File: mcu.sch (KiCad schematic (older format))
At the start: 74 parts, among them J10 JTAG, J11 esp32L, J12 esp32B, J13 esp32R, J2 SPI1, J3 uSD, J4 I2C1, J5 serial1, J6 serial2, J7 touch interface, J8 LCD 4.3, J9 EXT_IOS, Q1 ZXMN2F30FH, Q2 ZXMN2F30FH, Q3 ZXMN2F30FH, SW1 reset, SW7 on, U3 AT25SF641, U5 STM32F750Z8, U6 MP3302DJ-LF-P, U7 ESP32-WROOM-32, Y1 25MHz, Y2 32.768 kHz

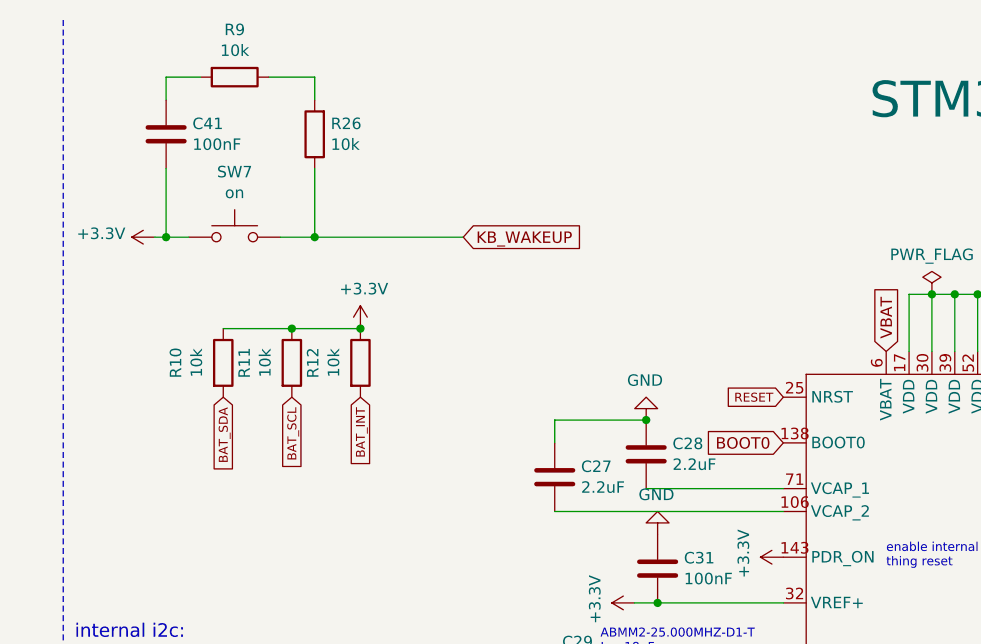
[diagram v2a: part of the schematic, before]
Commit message: Switch matrix to definitive switch
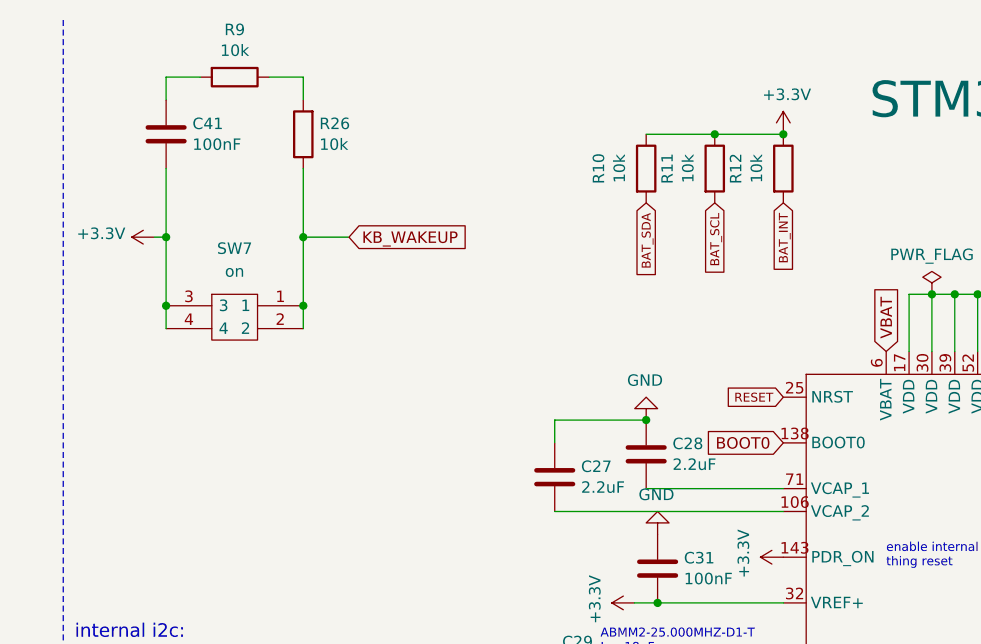
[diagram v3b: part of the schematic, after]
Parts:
- removed SW7: on, Button_Switch_THT:SW_PUSH_6mm, symbol Switch:SW_Push
- added SW7: on, SamacSys_Parts:FSM4JSMATR, symbol SamacSys_Parts:FSM4JSMAATR
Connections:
- net +3V3: now also SW7.3, SW7.4
- net KB_WAKEUP: now also SW7.1, SW7.2
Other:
- moved on the sheet: R10, R11, R12, R26
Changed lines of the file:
@@
 Text Notes 13100 5300 0    39   ~ 0
 USART6_TX
-Text GLabel 10900 2150 3    39   Input ~ 0
+Text GLabel 12750 1300 3    39   Input ~ 0
 BAT_INT
 $Comp
 L Device:R R12
 U 1 1 6021C497
-P 10900 2000
-F 0 "R12" V 10693 2000 50  0000 C CNN
-F 1 "10k" V 10784 2000 50  0000 C CNN
-F 2 "Resistor_SMD:R_0805_2012Metric_Pad1.20x1.40mm_HandSolder" V 10830 2000 50  0001 C CNN
-F 3 "~" H 10900 2000 50  0001 C CNN
-	1    10900 2000
+P 12750 1150
+F 0 "R12" V 12543 1150 50  0000 C CNN
+F 1 "10k" V 12634 1150 50  0000 C CNN
+F 2 "Resistor_SMD:R_0805_2012Metric_Pad1.20x1.40mm_HandSolder" V 12680 1150 50  0001 C CNN
+F 3 "~" H 12750 1150 50  0001 C CNN
+	1    12750 1150
 	1    0    0    -1
 $EndComp
@@
 L power:+3.3V #PWR0139
 U 1 1 6021C91D
-P 10900 1850
-F 0 "#PWR0139" H 10900 1700 50  0001 C CNN
-F 1 "+3.3V" H 10915 2023 50  0000 C CNN
-F 2 "" H 10900 1850 50  0001 C CNN
-F 3 "" H 10900 1850 50  0001 C CNN
-	1    10900 1850
-	1    0    0    -1
-$EndComp
-Text GLabel 10300 2150 3    39   Input ~ 0
+P 12750 1000
+F 0 "#PWR0139" H 12750 850 50  0001 C CNN
+F 1 "+3.3V" H 12765 1173 50  0000 C CNN
+F 2 "" H 12750 1000 50  0001 C CNN
+F 3 "" H 12750 1000 50  0001 C CNN
+	1    12750 1000
+	1    0    0    -1
+$EndComp
+Text GLabel 12150 1300 3    39   Input ~ 0
 BAT_SDA
-Text GLabel 10600 2150 3    39   Input ~ 0
+Text GLabel 12450 1300 3    39   Input ~ 0
 BAT_SCL
 $Comp
 L Device:R R11
 U 1 1 602407FE
-P 10600 2000
-F 0 "R11" V 10393 2000 50  0000 C CNN
-F 1 "10k" V 10484 2000 50  0000 C CNN
-F 2 "Resistor_SMD:R_0805_2012Metric_Pad1.20x1.40mm_HandSolder" V 10530 2000 50  0001 C CNN
-F 3 "~" H 10600 2000 50  0001 C CNN
-	1    10600 2000
+P 12450 1150
+F 0 "R11" V 12243 1150 50  0000 C CNN
+F 1 "10k" V 12334 1150 50  0000 C CNN
+F 2 "Resistor_SMD:R_0805_2012Metric_Pad1.20x1.40mm_HandSolder" V 12380 1150 50  0001 C CNN
+F 3 "~" H 12450 1150 50  0001 C CNN
+	1    12450 1150
 	1    0    0    -1
 $EndComp
@@
 L Device:R R10
 U 1 1 6024B53D
-P 10300 2000
-F 0 "R10" V 10093 2000 50  0000 C CNN
-F 1 "10k" V 10184 2000 50  0000 C CNN
-F 2 "Resistor_SMD:R_0805_2012Metric_Pad1.20x1.40mm_HandSolder" V 10230 2000 50  0001 C CNN
-F 3 "~" H 10300 2000 50  0001 C CNN
-	1    10300 2000
-	1    0    0    -1
-$EndComp
-Wire Wire Line
-	10300 1850 10600 1850
-Connection ~ 10900 1850
-Connection ~ 10600 1850
-Wire Wire Line
-	10600 1850 10900 1850
+P 12150 1150
+F 0 "R10" V 11943 1150 50  0000 C CNN
+F 1 "10k" V 12034 1150 50  0000 C CNN
+F 2 "Resistor_SMD:R_0805_2012Metric_Pad1.20x1.40mm_HandSolder" V 12080 1150 50  0001 C CNN
+F 3 "~" H 12150 1150 50  0001 C CNN
+	1    12150 1150
+	1    0    0    -1
+$EndComp
+Wire Wire Line
+	12150 1000 12450 1000
+Connection ~ 12750 1000
+Connection ~ 12450 1000
+Wire Wire Line
+	12450 1000 12750 1000
 $Comp
 L power:+3.3V #PWR0142
@@
 Text Notes 10550 10900 0    39   ~ 0
 R VF=1.8-2.4 FC=30\nG VF=2.8-3.9 FC=20\nB VF=2.8-3.9 FC=20\nSupply=3.3
-Text GLabel 11350 1450 2    50   Input ~ 0
+Text GLabel 10850 1450 2    50   Input ~ 0
 KB_WAKEUP
-$Comp
-L Switch:SW_Push SW7
-U 1 1 5F9751F4
-P 10350 1450
-F 0 "SW7" H 10350 1735 50  0000 C CNN
-F 1 "on" H 10350 1644 50  0000 C CNN
-F 2 "Button_Switch_THT:SW_PUSH_6mm" H 10350 1650 50  0001 C CNN
-F 3 "~" H 10350 1650 50  0001 C CNN
-	1    10350 1450
-	1    0    0    -1
-$EndComp
 Text Notes 9650 3500 0    59   ~ 0
 internal i2c:\n6BH - Battery charger\nBA/BB or 28/29 - Touch display\n20 - Keyboard matrix output
@@
 L Device:R R26
 U 1 1 5FA5B33C
-P 10700 1000
-F 0 "R26" H 10630 954 50  0000 R CNN
-F 1 "10k" H 10630 1045 50  0000 R CNN
-F 2 "Resistor_SMD:R_0805_2012Metric_Pad1.20x1.40mm_HandSolder" V 10630 1000 50  0001 C CNN
-F 3 "~" H 10700 1000 50  0001 C CNN
-	1    10700 1000
+P 10650 1000
+F 0 "R26" H 10580 954 50  0000 R CNN
+F 1 "10k" H 10580 1045 50  0000 R CNN
+F 2 "Resistor_SMD:R_0805_2012Metric_Pad1.20x1.40mm_HandSolder" V 10580 1000 50  0001 C CNN
+F 3 "~" H 10650 1000 50  0001 C CNN
+	1    10650 1000
 	-1   0    0    1
 $EndComp
@@
 	10000 1450 10050 1450
 Wire Wire Line
-	10550 1450 10700 1450
-Wire Wire Line
-	10500 750  10700 750
-Wire Wire Line
-	10700 750  10700 850
-Wire Wire Line
-	10700 1150 10700 1450
-Connection ~ 10700 1450
-Wire Wire Line
-	10700 1450 11350 1450
-Wire Wire Line
 	10050 1450 10050 1150
-Connection ~ 10050 1450
-Wire Wire Line
-	10050 1450 10150 1450
 Wire Wire Line
 	10050 850  10050 750
@@
 NoConn ~ 15050 3950
 NoConn ~ 12750 6750
+$Comp
+L SamacSys_Parts:FSM4JSMAATR SW7
+U 1 1 5F9A03CF
+P 10050 1750
+F 0 "SW7" H 10350 2000 50  0000 C CNN
+F 1 "on" H 10350 1900 50  0000 C CNN
+F 2 "SamacSys_Parts:FSM4JSMATR" H 11100 1850 50  0001 L CNN
+F 3 "http://www.te.com/commerce/DocumentDelivery/DDEController?Action=showdoc&DocId=Customer+Drawing%7F2-1437565-7%7FV%7Fpdf%7FEnglish%7FENG_CD_2-1437565-7_V.pdf%7F1571563-4" H 11100 1750 50  0001 L CNN
+F 4 "TE CONNECTIVITY / ALCOSWITCH - FSM4JSMAATR - TACTILE SWITCH, SPST-NO, 0.05A, 24V, SMD" H 11100 1650 50  0001 L CNN "Description"
+F 5 "" H 11100 1550 50  0001 L CNN "Height"
+F 6 "TE Connectivity" H 11100 1450 50  0001 L CNN "Manufacturer_Name"
+F 7 "FSM4JSMAATR" H 11100 1350 50  0001 L CNN "Manufacturer_Part_Number"
+F 8 "FSM4JSMAATR" H 11100 1250 50  0001 L CNN "Arrow Part Number"
+F 9 "https://www.arrow.com/en/products/fsm4jsmaatr/te-connectivity" H 11100 1150 50  0001 L CNN "Arrow Price/Stock"
+F 10 "506-FSM4JSMAATR" H 11100 1050 50  0001 L CNN "Mouser Part Number"
+F 11 "https://www.mouser.co.uk/ProductDetail/TE-Connectivity-PB/FSM4JSMAATR?qs=BaILwcusPn8tfgWWpzI4xg%3D%3D" H 11100 950 50  0001 L CNN "Mouser Price/Stock"
+	1    10050 1750
+	1    0    0    -1
+$EndComp
+Wire Wire Line
+	10050 1450 10050 1750
+Connection ~ 10050 1450
+Connection ~ 10050 1750
+Wire Wire Line
+	10050 1750 10050 1850
+Wire Wire Line
+	10650 1850 10650 1750
+Wire Wire Line
+	10650 1450 10850 1450
+Connection ~ 10650 1750
+Wire Wire Line
+	10650 1750 10650 1450
+Wire Wire Line
+	10650 1150 10650 1450
+Connection ~ 10650 1450
+Wire Wire Line
+	10500 750  10650 750
+Wire Wire Line
+	10650 750  10650 850
 $EndSCHEMATC

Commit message: Switch stuff around; Use two MCP
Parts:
- J4: footprint Connector_PinHeader_2.54mm:PinHeader_1x05_P2.54mm_Horizontal -> Connector_PinHeader_2.54mm:PinHeader_1x04_P2.54mm_Horizontal; symbol Connector_Generic:Conn_01x05 -> Connector_Generic:Conn_01x04
- J9: footprint Connector_PinHeader_2.54mm:PinHeader_1x06_P2.54mm_Horizontal -> Connector_PinHeader_2.54mm:PinHeader_1x08_P2.54mm_Horizontal; symbol Connector_Generic:Conn_02x03_Odd_Even -> Connector_Generic:Conn_02x04_Odd_Even
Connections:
- net KB_ROW_3 is gone; now on net EXTIO_3: U5.87 (PG2)
- net KB_ROW_4 is gone; now on net EXTIO_4: U5.88 (PG3)
- net +3V3: now also J4.4 (Pin_4); no longer J4.5 (Pin_5)
- net BOOT0: no longer U5.56 (PG0)
- net EXTIO_3: no longer U5.66 (PE13)
- net EXTIO_4: no longer U5.67 (PE14)
- net RGBLED1_B: now also U5.137 (PB7); no longer U5.114 (PD0)
- net RGBLED1_G: now also U5.135 (PB5); no longer U5.115 (PD1)
- net RGBLED1_R: now also U5.134 (PB4); no longer U5.118 (PD4)
- net EXTIO_1_PWM: now reaches U5.85 (PD14)
- net EXTIO_1_PWM: now also J9.3 (Pin_3)
- net EXTIO_2_PWM: now reaches U5.86 (PD15)
- net EXTIO_2_PWM: now also J9.4 (Pin_4)
- removed net EXTIO_1: J9.3 (Pin_3), U5.134 (PB4)
- net EXTIO_2: no longer names the net of U5.81 (PD12)
- net EXTIO_2: no longer J9.4 (Pin_4)
- net I2C1_SMBA: no longer names the net of U5.12 (PF2)
- net I2C1_SMBA: no longer J4.4 (Pin_4)
- net KB_ROW_10: no longer names the net of U5.142 (PE1)
- net KB_ROW_2: no longer names the net of U5.57 (PG1)
- net KB_ROW_5 renamed EXTIO_5
- net EXTIO_5: now also J9.7 (Pin_7)
- net KB_ROW_6 renamed EXTIO_6
- net EXTIO_6: now also J9.8 (Pin_8)
- net KB_ROW_7: no longer names the net of U5.91 (PG6)
- net KB_ROW_8: no longer names the net of U5.93 (PG8)
- net KB_ROW_9: no longer names the net of U5.141 (PE0)
- no-connect marks 29 -> 38
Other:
- note added: "in/out/pwm"
- note added: "internal i2c (bat_xxx):\n6BH - Battery charger\nBA/BB or 28/29 - Touch display\n20 - Keyboard matrix columns\n21 - Keyboard matrix rows"
- note added: "led out / pwm"
- note added: "pwm:\ntim4_ch3\ntim4_ch4"
- note removed: "COL are inputs, pull-up sw\nROW output"
- note removed: "I2C2_SMBA"
- note removed: "PWR On button is KB_COL_1 / KB_ROW_11\nESC button is KB_COL_12 / KB_ROW_1"
- note removed: "TIM3_CH1"
- note removed: "TIM4_CH1"
- note removed: "in or out"
- note removed: "internal i2c:\n6BH - Battery charger\nBA/BB or 28/29 - Touch display\n20 - Keyboard matrix output"
- note removed: "keyboard row in"
- note removed: "led out"
- note removed: "pwm"
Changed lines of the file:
@@
 Text GLabel 10550 9600 2    50   Input ~ 0
-RGBLED1_B
-Text GLabel 15050 7650 2    50   Input ~ 0
-RGBLED1_R
-Text GLabel 15050 7350 2    50   Input ~ 0
-RGBLED1_G
-Text GLabel 15050 7250 2    50   Input ~ 0
 RGBLED1_B
 $Comp
@@
 in blue text is\nthe function\nor alternate\nof the pin
 $Comp
-L Connector_Generic:Conn_01x05 J4
+L Connector_Generic:Conn_01x04 J4
 U 1 1 5F9E8C86
 P 1150 9500
 F 0 "J4" H 1068 9075 50  0000 C CNN
 F 1 "I2C1" H 1068 9166 50  0000 C CNN
-F 2 "Connector_PinHeader_2.54mm:PinHeader_1x05_P2.54mm_Horizontal" H 1150 9500 50  0001 C CNN
+F 2 "Connector_PinHeader_2.54mm:PinHeader_1x04_P2.54mm_Horizontal" H 1150 9500 50  0001 C CNN
 F 3 "~" H 1150 9500 50  0001 C CNN
 	1    1150 9500
@@
 L power:GND #PWR0114
 U 1 1 5F9F2110
-P 1350 9700
-F 0 "#PWR0114" H 1350 9450 50  0001 C CNN
-F 1 "GND" V 1355 9572 50  0000 R CNN
-F 2 "" H 1350 9700 50  0001 C CNN
-F 3 "" H 1350 9700 50  0001 C CNN
-	1    1350 9700
+P 1350 9600
+F 0 "#PWR0114" H 1350 9350 50  0001 C CNN
+F 1 "GND" V 1355 9472 50  0000 R CNN
+F 2 "" H 1350 9600 50  0001 C CNN
+F 3 "" H 1350 9600 50  0001 C CNN
+	1    1350 9600
 	0    -1   -1   0
 $EndComp
@@
 	0    1    1    0
 $EndComp
-Text GLabel 1350 9600 2    39   Input ~ 0
+Text GLabel 1350 9500 2    39   Input ~ 0
 I2C1_SDA
-Text GLabel 1350 9500 2    39   Input ~ 0
+Text GLabel 1350 9400 2    39   Input ~ 0
 I2C1_SCL
-Text GLabel 1350 9400 2    39   Input ~ 0
-I2C1_SMBA
 Text GLabel 1350 8700 2    39   Input ~ 0
 SPI1_MISO
@@
 Text Notes 13100 5700 0    39   ~ 0
 I2C2_SCL
-Text Notes 13100 5800 0    39   ~ 0
-I2C2_SMBA
-Text GLabel 12750 5750 0    39   Input ~ 0
-I2C1_SMBA
 Text GLabel 12750 5650 0    39   Input ~ 0
 I2C1_SCL
@@
 I2C1_SDA
 $Comp
-L Connector_Generic:Conn_02x03_Odd_Even J9
+L Connector_Generic:Conn_02x04_Odd_Even J9
 U 1 1 5FA5F870
 P 11100 8600
 F 0 "J9" H 11150 8917 50  0000 C CNN
 F 1 "EXT_IOS" H 11150 8826 50  0000 C CNN
-F 2 "Connector_PinHeader_2.54mm:PinHeader_1x06_P2.54mm_Horizontal" H 11100 8600 50  0001 C CNN
+F 2 "Connector_PinHeader_2.54mm:PinHeader_1x08_P2.54mm_Horizontal" H 11100 8600 50  0001 C CNN
 F 3 "~" H 11100 8600 50  0001 C CNN
 	1    11100 8600
@@
 $EndComp
 Text GLabel 10900 8600 0    39   Input ~ 0
-EXTIO_1
+EXTIO_1_PWM
 Text GLabel 10900 8700 0    39   Input ~ 0
 EXTIO_3
@@
 EXTIO_4
 Text GLabel 11400 8600 2    39   Input ~ 0
-EXTIO_2
+EXTIO_2_PWM
 Text Notes 14400 7800 0    39   ~ 0
 USART2_TX
@@
 	1    0    0    -1
 $EndComp
-Text GLabel 12750 4650 0    50   Input ~ 0
-KB_ROW_8
-Text GLabel 12750 4450 0    50   Input ~ 0
-KB_ROW_7
-Text GLabel 12750 4350 0    50   Input ~ 0
-KB_ROW_6
-Text GLabel 12750 4250 0    50   Input ~ 0
-KB_ROW_5
-Text GLabel 12750 4150 0    50   Input ~ 0
-KB_ROW_4
-Text GLabel 12750 4050 0    50   Input ~ 0
-KB_ROW_3
-Text GLabel 12750 3950 0    50   Input ~ 0
-KB_ROW_2
-Text GLabel 12750 3850 0    50   Input ~ 0
-KB_ROW_1
-Text GLabel 12750 7250 0    50   Input ~ 0
-KB_ROW_9
-Text GLabel 12750 7350 0    50   Input ~ 0
-KB_ROW_10
 Text GLabel 15050 2150 2    50   Input ~ 0
 KB_WAKEUP
-Text Notes 3750 10750 0    118  ~ 0
-PWR On button is KB_COL_1 / KB_ROW_11\nESC button is KB_COL_12 / KB_ROW_1
 Text GLabel 3000 9050 0    50   Input ~ 0
 KB_COL_12
@@
 Text Notes 600  11100 0    98   ~ 0
 TODO to validate:\n- BOOT0 behavior\n- WAKEUP through ON behavior\n- RESET
-Text Notes 15500 4300 0    39   ~ 0
-TIM3_CH1
-Text Notes 3750 11050 0    79   ~ 0
-COL are inputs, pull-up sw\nROW output
-Text Notes 13050 3900 0    39   ~ 0
-keyboard row in
-Text Notes 13050 4000 0    39   ~ 0
-keyboard row in
-Text Notes 13050 4100 0    39   ~ 0
-keyboard row in
-Text Notes 13050 4200 0    39   ~ 0
-keyboard row in
-Text Notes 13050 4300 0    39   ~ 0
-keyboard row in
-Text Notes 13050 4400 0    39   ~ 0
-keyboard row in
-Text Notes 13050 4500 0    39   ~ 0
-keyboard row in
-Text Notes 13050 7300 0    39   ~ 0
-keyboard row in
-Text Notes 13050 4700 0    39   ~ 0
-keyboard row in
-Text Notes 13050 7400 0    39   ~ 0
-keyboard row in
 Text GLabel 12750 4750 0    39   Input ~ 0
 SERIAL3_RX
@@
 Text GLabel 15050 4150 2    39   Input ~ 0
 JTDO
-Text GLabel 15050 4250 2    39   Input ~ 0
-EXTIO_1
-Text GLabel 15050 8450 2    39   Input ~ 0
-EXTIO_2
 Text GLabel 12750 7050 0    39   Input ~ 0
 BAT_SDA
@@
 Text Notes 13100 6900 0    39   ~ 0
 i/o
-Text Notes 13100 8700 0    39   ~ 0
-in or out
-Text Notes 14450 4300 0    39   ~ 0
-in or out
-Text Notes 13100 8600 0    39   ~ 0
-in or out
-Text Notes 14400 8500 0    39   ~ 0
-in or out
 Text Notes 13050 4600 0    39   ~ 0
 LCD_CLK
 Text Notes 14400 6200 0    39   ~ 0
 LCD_HSYNC
-Text Notes 14550 7400 0    39   ~ 0
-led out
-Text Notes 14500 7700 0    39   ~ 0
-led out
-Text Notes 14550 7300 0    39   ~ 0
-led out
 Text Notes 14600 4200 0    39   ~ 0
 JTDO
@@
 Text Notes 14450 2600 0    39   ~ 0
 LCD_VSYNC
-Text Notes 15350 4300 0    39   ~ 0
-pwm
-Text Notes 15350 8500 0    39   ~ 0
-pwm
-Text GLabel 12750 8650 0    39   Input ~ 0
-EXTIO_4
-Text GLabel 12750 8550 0    39   Input ~ 0
-EXTIO_3
 Text Notes 14600 2900 0    39   ~ 0
 input
-Text Notes 15500 8500 0    39   ~ 0
-TIM4_CH1
 Text Notes 13100 8200 0    39   ~ 0
 TIM1_CH1
@@
 Text Notes 13200 2900 0    39   ~ 0
 enable internal power\nthing reset
-NoConn ~ 15050 4350
-NoConn ~ 15050 4550
 NoConn ~ 12750 5350
 NoConn ~ 15050 6850
 NoConn ~ 15050 7950
-NoConn ~ 15050 8250
 NoConn ~ 15050 8550
-$Comp
-L power:PWR_FLAG #FLG0101
-U 1 1 603049DE
-P 13400 1700
-F 0 "#FLG0101" H 13400 1775 50  0001 C CNN
-F 1 "PWR_FLAG" H 13400 1873 50  0000 C CNN
-F 2 "" H 13400 1700 50  0001 C CNN
-F 3 "~" H 13400 1700 50  0001 C CNN
-	1    13400 1700
-	1    0    0    -1
-$EndComp
 Text Notes 700  7150 0    118  ~ 0
 serial / i2c / etc
@@
 Wire Notes Line
 	3850 5000 3850 8450
-Text Notes 10600 9200 0    118  ~ 0
+Text Notes 10600 9300 0    118  ~ 0
 RGB Led status
 Text Notes 8300 8250 0    118  ~ 0
@@
 	7050 7950 12200 7950
 Wire Notes Line
-	12200 8800 10250 8800
-Wire Notes Line
 	7050 7500 7050 9950
 $Comp
@@
 $EndComp
 Wire Wire Line
-	6450 6000 5900 6000
+	6450 6000 6250 6000
 Connection ~ 5900 6000
 Wire Wire Line
@@
 Connection ~ 7250 6700
 Wire Wire Line
-	7250 6700 6450 6700
+	7250 6700 6750 6700
 Wire Wire Line
 	7200 7100 7250 7100
@@
 ABS07-166-32.768KHZ-T
 $Comp
-L d_st:STM32F750Z8 U5
-U 1 1 5F863DEB
-P 13900 2050
-F 0 "U5" H 13900 -500 157 0000 C CNN
-F 1 "STM32F750Z8" H 13900 3250 157 0000 C CNN
-F 2 "Package_QFP:LQFP-144_20x20mm_P0.5mm" H 13800 2200 157 0001 C CNN
-F 3 "" H 13800 2200 157 0001 C CNN
-F 4 "C411817" H 13900 2050 50  0001 C CNN "lcsc"
-	1    13900 2050
-	1    0    0    -1
-$EndComp
-$Comp
 L Device:C_Small C29
 U 1 1 6102D7D8
@@
 KB_WAKEUP
 Text Notes 9650 3500 0    59   ~ 0
-internal i2c:\n6BH - Battery charger\nBA/BB or 28/29 - Touch display\n20 - Keyboard matrix output
+internal i2c (bat_xxx):\n6BH - Battery charger\nBA/BB or 28/29 - Touch display\n20 - Keyboard matrix columns\n21 - Keyboard matrix rows
 $Comp
 L power:+3.3V #PWR0111
@@
 NoConn ~ 12750 7550
 NoConn ~ 12750 8250
-NoConn ~ 15050 8650
-NoConn ~ 15050 8750
 NoConn ~ 15050 3950
 NoConn ~ 12750 6750
@@
 Wire Wire Line
 	10650 750  10650 850
+NoConn ~ 12750 5750
+$Comp
+L d_st:STM32F750Z8 U5
+U 1 1 5F863DEB
+P 13900 2050
+F 0 "U5" H 13900 -500 157 0000 C CNN
+F 1 "STM32F750Z8" H 13900 3250 157 0000 C CNN
+F 2 "Package_QFP:LQFP-144_20x20mm_P0.5mm" H 13800 2200 157 0001 C CNN
+F 3 "" H 13800 2200 157 0001 C CNN
+F 4 "C411817" H 13900 2050 50  0001 C CNN "lcsc"
+	1    13900 2050
+	1    0    0    -1
+$EndComp
+Text GLabel 15050 8650 2    39   Input ~ 0
+EXTIO_1_PWM
+Text Notes 14350 8650 0    39   ~ 0
+in/out/pwm
+Text GLabel 15050 8750 2    39   Input ~ 0
+EXTIO_2_PWM
+Text Notes 14350 8750 0    39   ~ 0
+in/out/pwm
+Text Notes 15550 8800 0    59   ~ 0
+pwm:\ntim4_ch3\ntim4_ch4
+Wire Notes Line
+	10250 9050 12200 9050
+Text GLabel 10900 8800 0    39   Input ~ 0
+EXTIO_5
+Text GLabel 11400 8800 2    39   Input ~ 0
+EXTIO_6
+Text GLabel 12750 4050 0    39   Input ~ 0
+EXTIO_3
+Text GLabel 12750 4150 0    39   Input ~ 0
+EXTIO_4
+Text GLabel 12750 4250 0    39   Input ~ 0
+EXTIO_5
+Text GLabel 12750 4350 0    39   Input ~ 0
+EXTIO_6
+Text GLabel 15050 4550 2    50   Input ~ 0
+RGBLED1_B
+Text GLabel 15050 4350 2    50   Input ~ 0
+RGBLED1_G
+Text GLabel 15050 4250 2    50   Input ~ 0
+RGBLED1_R
+Text Notes 14300 4300 0    39   ~ 0
+led out / pwm
+Text Notes 14300 4400 0    39   ~ 0
+led out / pwm
+Text Notes 14300 4600 0    39   ~ 0
+led out / pwm
+NoConn ~ 12750 3850
+NoConn ~ 12750 3950
+NoConn ~ 12750 4450
+NoConn ~ 12750 4650
+NoConn ~ 12750 7250
+NoConn ~ 12750 7350
+NoConn ~ 12750 8550
+NoConn ~ 12750 8650
+NoConn ~ 15050 8450
+NoConn ~ 15050 8250
+NoConn ~ 15050 7250
+NoConn ~ 15050 7350
+NoConn ~ 15050 7650
+$Comp
+L power:PWR_FLAG #FLG0105
+U 1 1 61831313
+P 6750 6700
+F 0 "#FLG0105" H 6750 6775 50  0001 C CNN
+F 1 "PWR_FLAG" H 6750 6873 50  0000 C CNN
+F 2 "" H 6750 6700 50  0001 C CNN
+F 3 "~" H 6750 6700 50  0001 C CNN
+	1    6750 6700
+	1    0    0    -1
+$EndComp
+Connection ~ 6750 6700
+Wire Wire Line
+	6750 6700 6450 6700
+$Comp
+L power:PWR_FLAG #FLG0106
+U 1 1 6183251A
+P 6250 6000
+F 0 "#FLG0106" H 6250 6075 50  0001 C CNN
+F 1 "PWR_FLAG" H 6250 6173 50  0000 C CNN
+F 2 "" H 6250 6000 50  0001 C CNN
+F 3 "~" H 6250 6000 50  0001 C CNN
+	1    6250 6000
+	1    0    0    -1
+$EndComp
+Connection ~ 6250 6000
+Wire Wire Line
+	6250 6000 5900 6000
 $EndSCHEMATC
